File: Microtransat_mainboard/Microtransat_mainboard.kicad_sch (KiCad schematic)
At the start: 29 parts, among them IC1 HT7833, J1 Conn_01x03, J10 Conn_01x04, J2 Conn_01x02, J3 Conn_01x03, J4 Conn_01x04, J5 Conn_01x05, J6 Conn_01x05, J7 Conn_01x05, J8 Conn_01x03, J9 Conn_01x04, SW1 SW_SPST, U1 LM2596, U5 SD Card Module

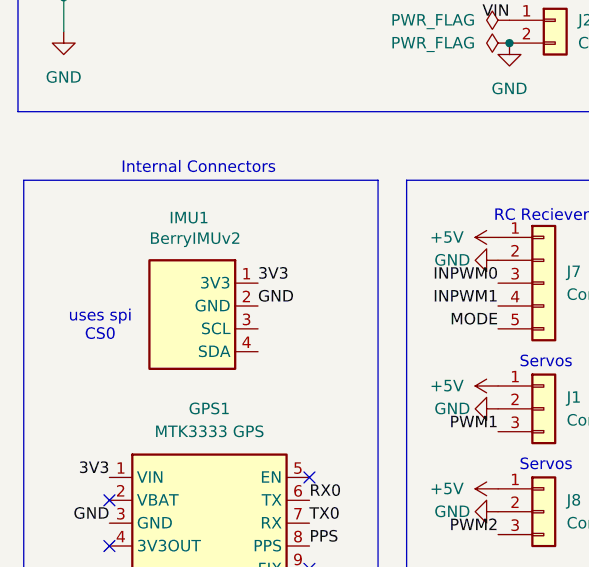
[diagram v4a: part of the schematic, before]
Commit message: Updated IMU symbol
V2 -> V3 SPI
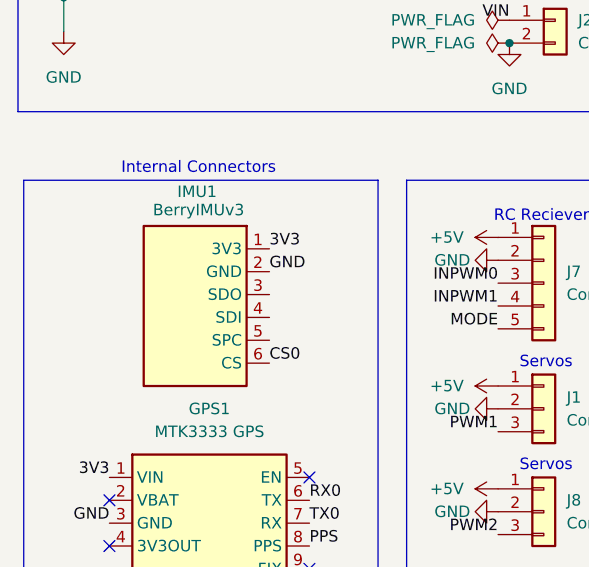
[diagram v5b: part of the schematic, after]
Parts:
- GPS1: footprint (none) -> footprints:MTK3333
- IMU1: value BerryIMUv2 -> BerryIMUv3; footprint (none) -> footprints:BerryIMUv3
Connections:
- net CS0: now also IMU1.6 (CS)
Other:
- note removed: "uses spi CS0"
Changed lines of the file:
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@@
 		)
 	)
-	(text "uses spi\nCS0\n"
-		(exclude_from_sim no)
-		(at 28.194 136.906 0)
-		(effects
-			(font
-				(size 1.27 1.27)
-			)
-		)
-	)
 	(text "RC Reciever"
 		(exclude_from_sim no)
@@
 	)
 	(label "GND"
-		(at 45.72 134.62 0)
+		(at 46.99 130.81 0)
 		(effects
 			(font
@@
 	)
 	(label "3V3"
-		(at 45.72 132.08 0)
+		(at 46.99 128.27 0)
 		(effects
 			(font
@@
 		)
 	)
+	(label "CS0"
+		(at 46.99 140.97 0)
+		(effects
+			(font
+				(size 1.27 1.27)
+			)
+			(justify left bottom)
+		)
+	)
 	(label "5B"
 		(at 111.76 186.69 180)
@@
 			)
 		)
-		(property "Footprint" ""
+		(property "Footprint" "footprints:MTK3333"
 			(at 37.465 157.48 0)
 			(effects
@@
 	(symbol
 		(lib_id "Microtransat:BerryIMUv2")
-		(at 37.465 127 0)
+		(at 38.1 123.19 0)
 		(mirror y)
 		(unit 1)
@@
 		(dnp no)
 		(property "Reference" "IMU1"
-			(at 40.259 124.841 0)
+			(at 41.148 121.92 0)
 			(effects
 				(font
@@
 			)
 		)
-		(property "Value" "BerryIMUv2"
-			(at 43.815 127.127 0)
+		(property "Value" "BerryIMUv3"
+			(at 44.196 123.952 0)
 			(effects
 				(font
@@
 			)
 		)
-		(property "Footprint" ""
-			(at 37.465 127 0)
+		(property "Footprint" "footprints:BerryIMUv3"
+			(at 38.1 123.19 0)
 			(effects
 				(font
@@
 		)
 		(property "Datasheet" ""
-			(at 37.465 127 0)
+			(at 38.1 123.19 0)
 			(effects
 				(font
@@
 		)
 		(property "Description" ""
-			(at 37.465 127 0)
+			(at 38.1 123.19 0)
 			(effects
 				(font
@@
 		(pin "4"
 		)
+		(pin "5"
+		)
+		(pin "6"
+		)
 		(instances

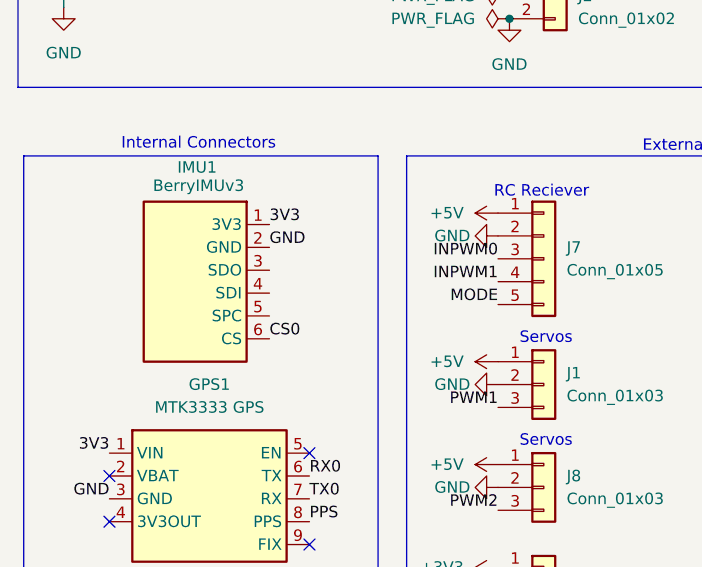
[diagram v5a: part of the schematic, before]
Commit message: Fixed library paths to project environment variable
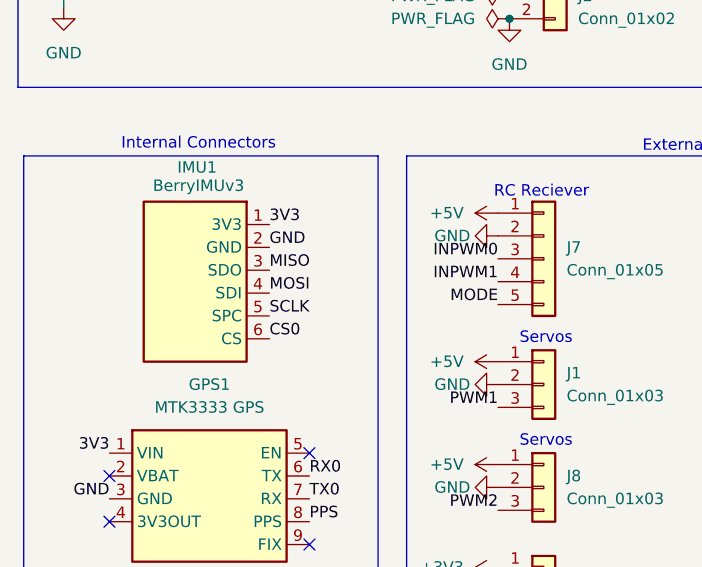
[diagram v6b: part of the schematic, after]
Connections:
- net MISO: now also IMU1.3 (SDO)
- net MOSI: now also IMU1.4 (SDI)
- net SCLK: now also IMU1.5 (SPC)
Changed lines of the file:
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@@
+		)
+	)
+	(label "SCLK"
+		(at 46.99 138.43 0)
+		(effects
+			(font
+				(size 1.27 1.27)
+			)
+			(justify left bottom)
 		)
 	)
@@
 		)
 	)
+	(label "MISO"
+		(at 46.99 133.35 0)
+		(effects
+			(font
+				(size 1.27 1.27)
+			)
+			(justify left bottom)
+		)
+	)
 	(label "LED1"
 		(at 217.17 34.29 180)
@@
 		)
 	)
+	(label "MOSI"
+		(at 46.99 135.89 0)
+		(effects
+			(font
+				(size 1.27 1.27)
+			)
+			(justify left bottom)
+		)
+	)
